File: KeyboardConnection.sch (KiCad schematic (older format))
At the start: 4 parts

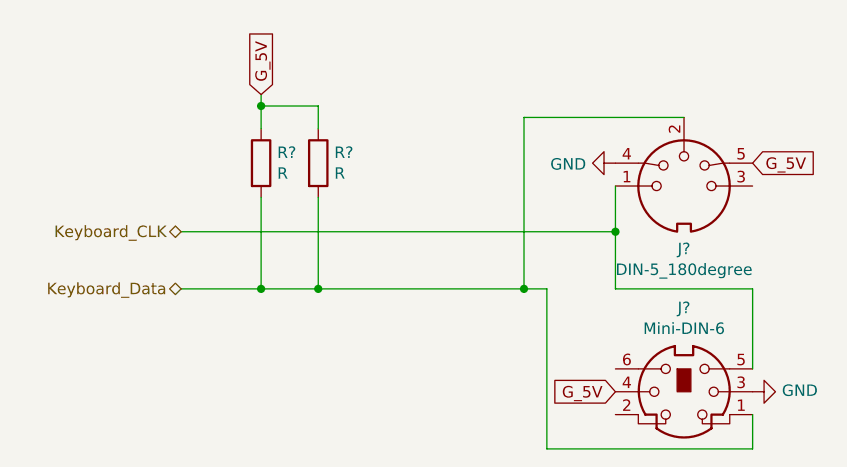
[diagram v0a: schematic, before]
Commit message: added the needed footprints
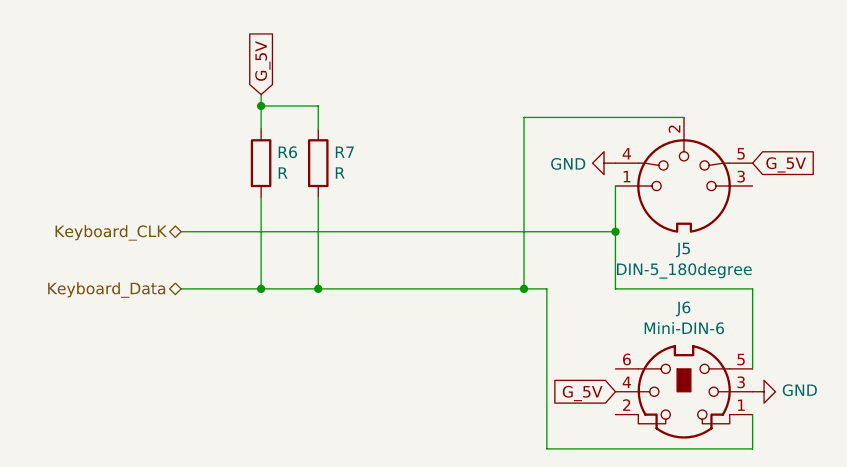
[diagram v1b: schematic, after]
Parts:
- R6, R7: renamed from R?; footprint (none) -> Resistor_THT:R_Axial_DIN0207_L6.3mm_D2.5mm_P7.62mm_Horizontal
- gave numbers to parts that had none: 2
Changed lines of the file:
@@
 Keyboard_Data
 $Comp
-L Connector:DIN-5_180degree J?
+L Connector:DIN-5_180degree J5
 U 1 1 5FC58202
 P 5300 2900
-F 0 "J?" H 5300 2625 50  0000 C CNN
+F 0 "J5" H 5300 2625 50  0000 C CNN
 F 1 "DIN-5_180degree" H 5300 2534 50  0000 C CNN
 F 2 "" H 5300 2900 50  0001 C CNN
@@
 $EndComp
 $Comp
-L Connector:Mini-DIN-6 J?
+L Connector:Mini-DIN-6 J6
 U 1 1 5FC5A9CE
 P 5300 3800
-F 0 "J?" H 5300 4167 50  0000 C CNN
+F 0 "J6" H 5300 4167 50  0000 C CNN
 F 1 "Mini-DIN-6" H 5300 4076 50  0000 C CNN
 F 2 "" H 5300 3800 50  0001 C CNN
@@
 	4600 3350 4700 3350
 $Comp
-L Device:R R?
+L Device:R R6
 U 1 1 5FC613DE
 P 3450 2800
-F 0 "R?" H 3520 2846 50  0000 L CNN
+F 0 "R6" H 3520 2846 50  0000 L CNN
 F 1 "R" H 3520 2755 50  0000 L CNN
-F 2 "" V 3380 2800 50  0001 C CNN
+F 2 "Resistor_THT:R_Axial_DIN0207_L6.3mm_D2.5mm_P7.62mm_Horizontal" V 3380 2800 50  0001 C CNN
 F 3 "~" H 3450 2800 50  0001 C CNN
 	1    3450 2800
@@
 $EndComp
 $Comp
-L Device:R R?
+L Device:R R7
 U 1 1 5FC621F3
 P 3700 2800
-F 0 "R?" H 3770 2846 50  0000 L CNN
+F 0 "R7" H 3770 2846 50  0000 L CNN
 F 1 "R" H 3770 2755 50  0000 L CNN
-F 2 "" V 3630 2800 50  0001 C CNN
+F 2 "Resistor_THT:R_Axial_DIN0207_L6.3mm_D2.5mm_P7.62mm_Horizontal" V 3630 2800 50  0001 C CNN
 F 3 "~" H 3700 2800 50  0001 C CNN
 	1    3700 2800
@@
 	3450 2550 3450 2500
 $Comp
-L power:GND #PWR?
+L power:GND #PWR019
 U 1 1 5FD05695
 P 5000 2800
-F 0 "#PWR?" H 5000 2550 50  0001 C CNN
+F 0 "#PWR019" H 5000 2550 50  0001 C CNN
 F 1 "GND" V 5005 2672 50  0000 R CNN
 F 2 "" H 5000 2800 50  0001 C CNN
@@
 $EndComp
 $Comp
-L power:GND #PWR?
+L power:GND #PWR020
 U 1 1 5FD05B03
 P 5600 3800
-F 0 "#PWR?" H 5600 3550 50  0001 C CNN
+F 0 "#PWR020" H 5600 3550 50  0001 C CNN
 F 1 "GND" V 5605 3672 50  0000 R CNN
 F 2 "" H 5600 3800 50  0001 C CNN

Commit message: layout time
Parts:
- J5: value DIN-5_180degree -> KeyboadDin5; footprint (none) -> LocalFootPrints:DIN5_midi
- J6: value Mini-DIN-6 -> KeyboardMiniDin6; footprint (none) -> LocalFootPrints:MiniDin6
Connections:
- net Keyboard_CLK: now also R7.2
- net Keyboard_Data: no longer R7.2
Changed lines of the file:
@@
 P 5300 2900
 F 0 "J5" H 5300 2625 50  0000 C CNN
-F 1 "DIN-5_180degree" H 5300 2534 50  0000 C CNN
-F 2 "" H 5300 2900 50  0001 C CNN
+F 1 "KeyboadDin5" H 5300 2534 50  0000 C CNN
+F 2 "LocalFootPrints:DIN5_midi" H 5300 2900 50  0001 C CNN
 F 3 "http://www.mouser.com/ds/2/18/40_c091_abd_e-75918.pdf" H 5300 2900 50  0001 C CNN
 	1    5300 2900
@@
 P 5300 3800
 F 0 "J6" H 5300 4167 50  0000 C CNN
-F 1 "Mini-DIN-6" H 5300 4076 50  0000 C CNN
-F 2 "" H 5300 3800 50  0001 C CNN
+F 1 "KeyboardMiniDin6" H 5300 4076 50  0000 C CNN
+F 2 "LocalFootPrints:MiniDin6" H 5300 3800 50  0001 C CNN
 F 3 "http://service.powerdynamics.com/ec/Catalog17/Section%2011.pdf" H 5300 3800 50  0001 C CNN
 	1    5300 3800
@@
 G_5V
 Wire Wire Line
-	3100 3100 5000 3100
+	3100 3100 3700 3100
 Wire Wire Line
 	5000 3100 5000 2900
@@
 Connection ~ 3450 3350
 Wire Wire Line
-	3450 3350 3700 3350
-Wire Wire Line
 	3450 2650 3450 2550
-Wire Wire Line
-	3700 3350 3700 2950
-Connection ~ 3700 3350
-Wire Wire Line
-	3700 3350 4600 3350
 Wire Wire Line
 	3700 2650 3700 2550
@@
 	0    -1   -1   0
 $EndComp
+Wire Wire Line
+	3450 3350 4600 3350
+Wire Wire Line
+	3700 2950 3700 3100
+Connection ~ 3700 3100
+Wire Wire Line
+	3700 3100 5000 3100
 $EndSCHEMATC
